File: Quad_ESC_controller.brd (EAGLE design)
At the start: 22.9 x 34 mm, 23 parts, among them Y1 ECS-80-S-4X

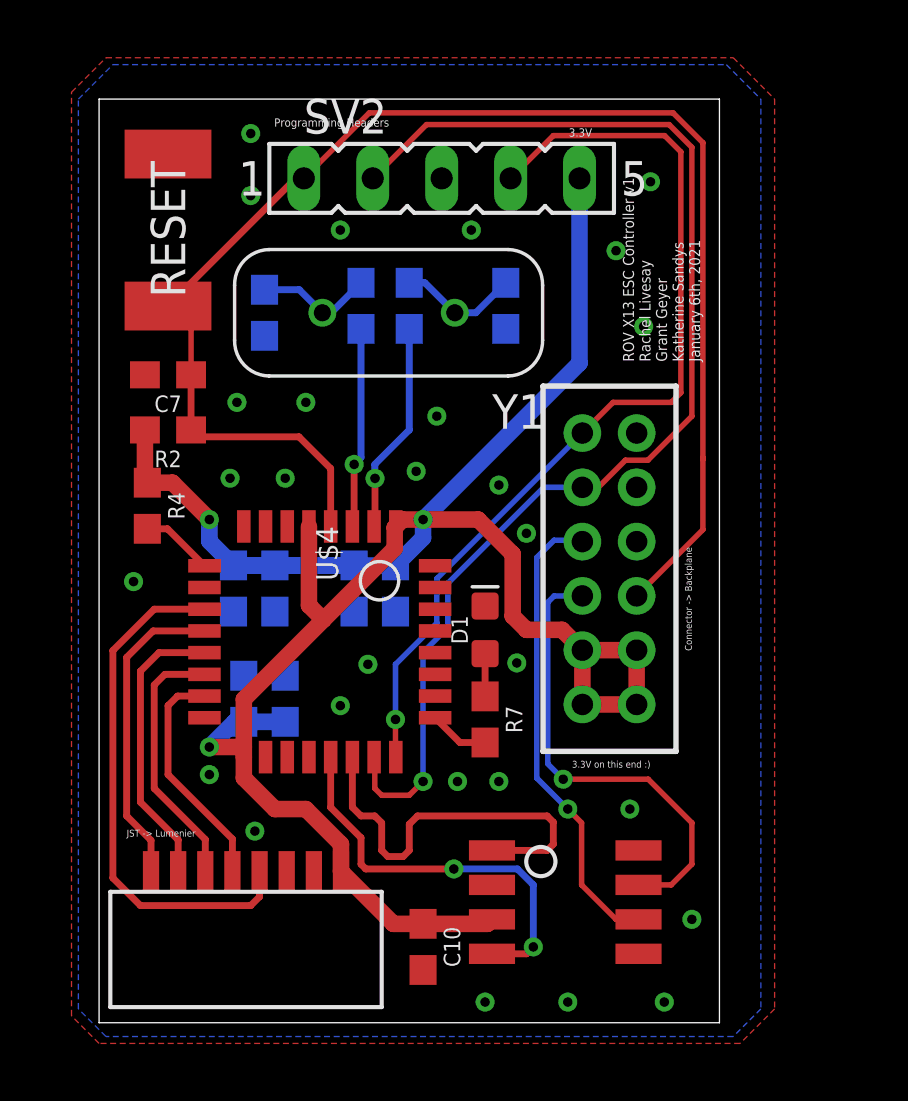
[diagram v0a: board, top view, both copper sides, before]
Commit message: Final Board Changes   ✽-(ˆ▿ˆ)/✽
thank god

(changes: vias con. to GND, esc id/tlm connections, design moved, connector footprint replaced, font sizes changed)
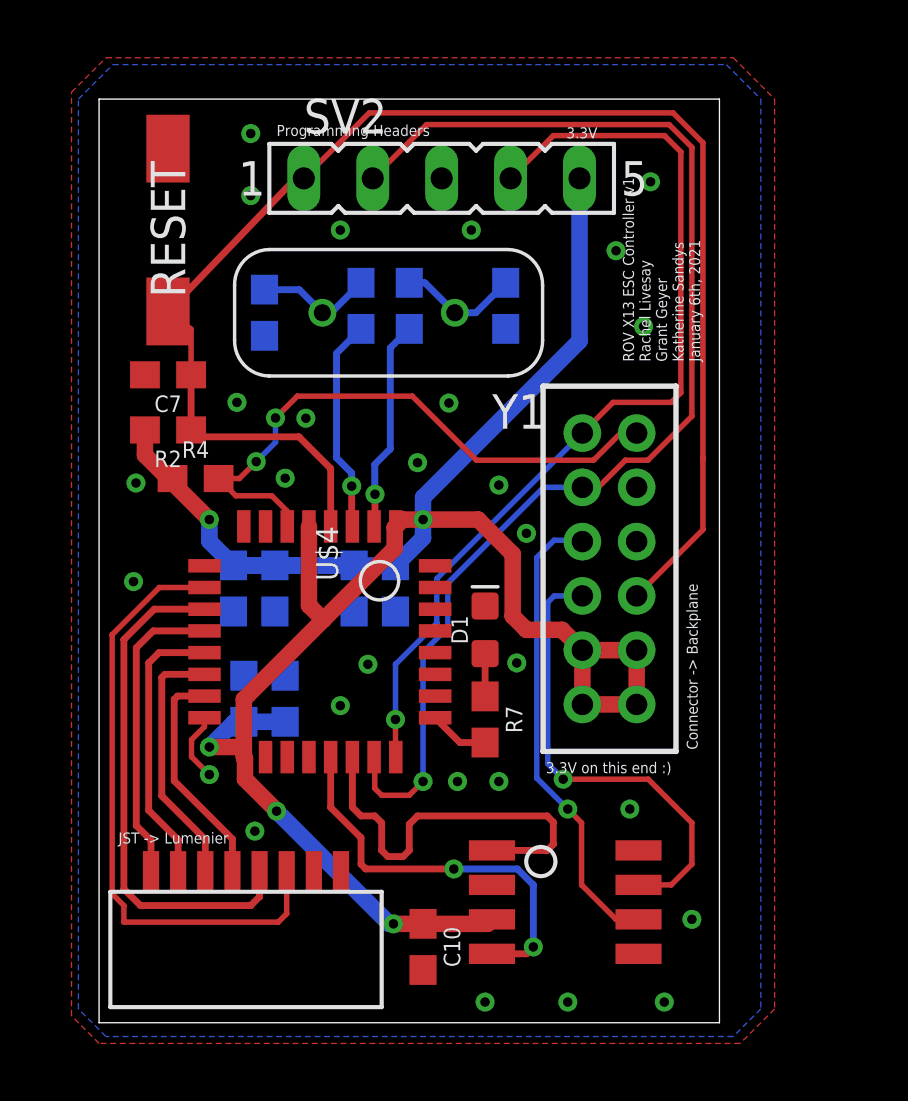
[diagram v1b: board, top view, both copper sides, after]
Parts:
- R7: value (none) -> 470
- RESET: value (none) -> DISCRETECOMPONENTS_SWITCH; device DiscreteComponents:SW_2512 -> Push button - FSM2JMTR:DISCRETECOMPONENTS_SW_2512
- U$3: value BACKPLANE_CONNECTORSBKP -> BACKPLANE_CONNECTORSESC; device BLHeli_32 45A:BACKPLANE_CONNECTORS_BKP -> BLHeli_32 45A:BACKPLANE_CONNECTORS_ESC
- moved R4 2.04 mm to (3.56, 20.1), turned to 0 degrees
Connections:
- removed net N$3: R4.2, U$4.PA3
- removed net N$7: U$3.8
- removed net N$8: U$3.12
- new net ADC: U$2.P$3, U$4.PA4
- new net ESC_ID: R4.2, U$3.12, U$4.PA0
- net +3V3: no longer U$2.P$1
- net GND: now also U$3.10; no longer U$2.P$3
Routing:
- net ADC: track 0.00 -> 22.6 mm
- net ESC_ID: track 0.00 -> 22.2 mm, vias 0 -> 2
- net N$3: track 2.67 -> 0.00 mm
- net GND: track 0.00 -> 2.56 mm, vias 0 -> 28
- net +3V3: track 85.9 -> 85.0 mm, vias 3 -> 5

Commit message: JST part
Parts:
- C10: value 100nF -> 0.1uF
- C8, C9: value 4.7uF -> 20pF
- R1, R3: value 1k -> 0
- U$2: value 8PIN_CONNECTOR -> JST-8PIN; device BLHeli_32 45A:8PI_CONNECTOR -> JST 8 pin:8PIN_CONNECTOR
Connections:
- net ADC: now also U$2.3; no longer U$2.P$3
- net GND: now also U$2.2; no longer U$2.P$2
- net TIM3_CH1: now also U$2.5; no longer U$2.P$5
- net TIM3_CH2: now also U$2.6; no longer U$2.P$6
- net TIM3_CH3: now also U$2.7; no longer U$2.P$7
- net TIM3_CH4: now also U$2.8; no longer U$2.P$8
- net TLM: now also U$2.4; no longer U$2.P$4

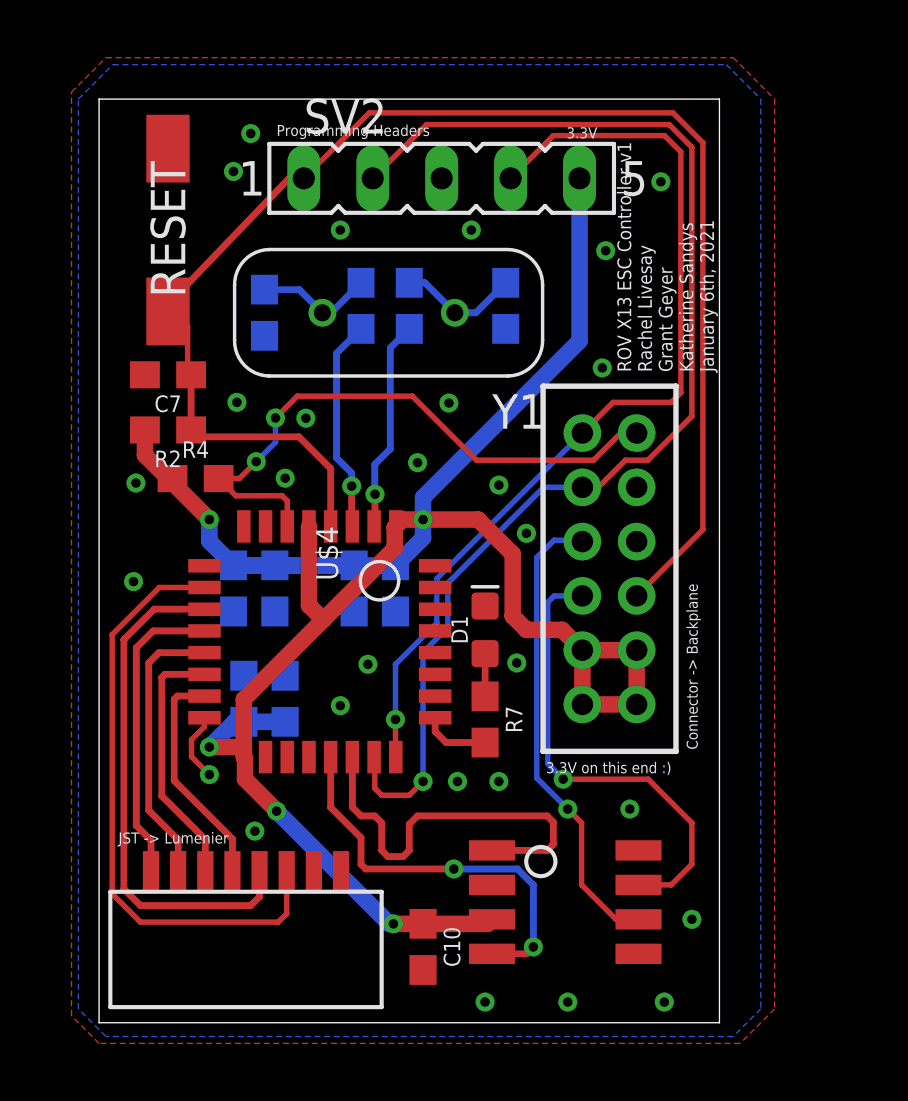
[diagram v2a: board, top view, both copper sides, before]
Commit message: Final Board Changes Pt. 2: Electric Boogaloo
Changes: [ bumped out board 100mil to the left, flipped esc signals on micro, moved TLM to analog pin 10 on micro, rotated connector, and rerouted board. ]
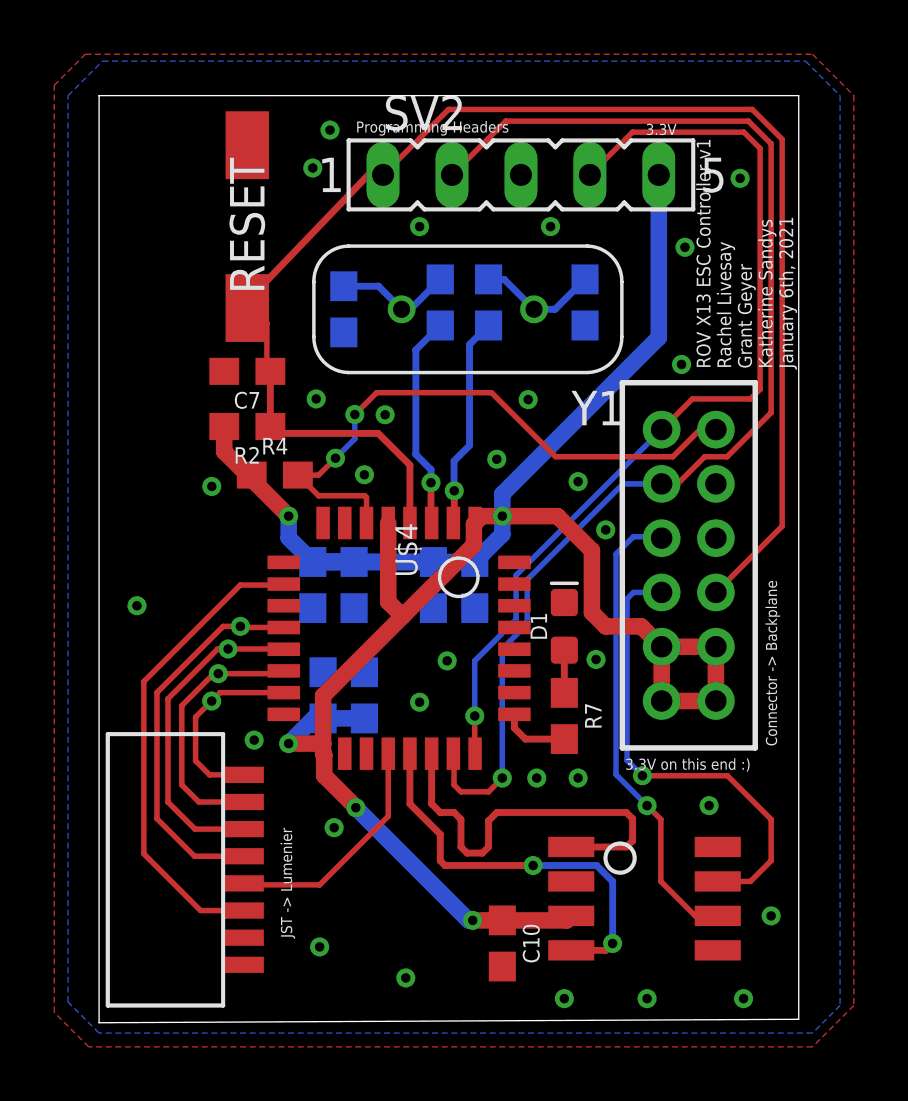
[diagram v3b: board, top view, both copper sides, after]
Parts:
- moved U$2 7.19 mm to (4.57, 0.64), turned to 90 degrees
- moved C3 2.92 mm to (12.3, 16.1)
- moved C4 2.92 mm to (8.26, 12.1)
- moved R1 2.92 mm to (12.6, 26.5)
- moved R3 2.92 mm to (14.4, 26.5)
- moved SV2 2.92 mm to (15.5, 31.2)
- moved U$4 2.92 mm to (8.26, 18.4)
- moved U$8 2.92 mm to (17.4, 2.67)
- moved Y1 2.92 mm to (13.6, 26.3)
- moved C2 2.92 mm to (9.78, 12.1)
- moved C7 2.92 mm to (5.46, 24.0)
- moved R2 2.92 mm to (5.46, 22.0)
- moved R4 2.92 mm to (6.48, 20.2)
- moved RESET 2.92 mm to (5.46, 29.3)
- moved C1 2.92 mm to (13.8, 16.1)
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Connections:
- net TIM3_CH1: now also U$4.PA6; no longer U$4.PB1
- net TIM3_CH2: now also U$4.PA7; no longer U$4.PB0
- net TIM3_CH3: now also U$4.PB0; no longer U$4.PA7
- net TIM3_CH4: now also U$4.PB1; no longer U$4.PA6
- net TLM: now also U$4.PA10; no longer U$4.PA5
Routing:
- net TLM: track 18.9 -> 8.71 mm
- net TIM3_CH1: track 8.39 -> 14.1 mm, vias 0 -> 1
- net ADC: track 22.2 -> 17.5 mm
- net TIM3_CH4: track 11.2 -> 7.21 mm, vias 0 -> 1
- net TIM3_CH2: track 9.43 -> 12.0 mm, vias 0 -> 1
- net GND: track 2.56 -> 0.00 mm, vias 28 -> 30
- net TIM3_CH3: track 10.3 -> 9.74 mm, vias 0 -> 1
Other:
- board size 22.9 x 34 mm -> 25.8 x 34.2 mm

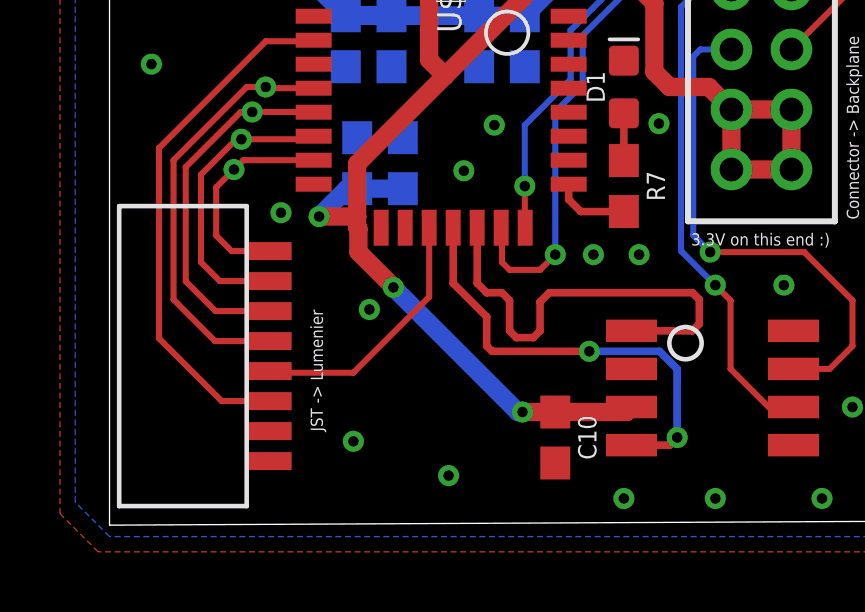
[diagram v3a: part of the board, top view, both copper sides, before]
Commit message: Added 1k Resistor TLM -> 3.3V
also tried airwiring it lol. it's v bad, but that is next year's problem.
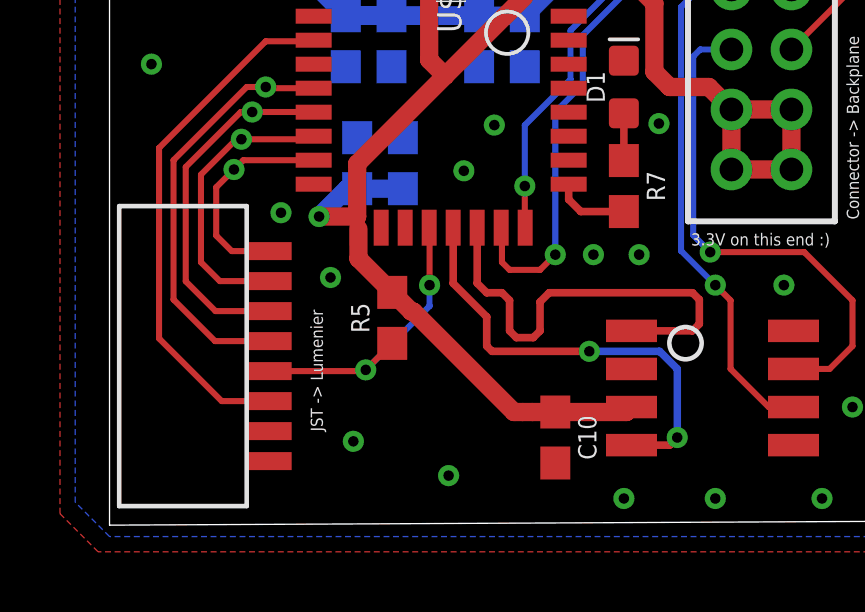
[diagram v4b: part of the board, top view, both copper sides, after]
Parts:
- added R5: 1k, SparkFun-Resistors:0603
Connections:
- net +3V3: now also R5.2
- net TLM: now also R5.1
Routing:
- net TLM: track 8.71 -> 10.2 mm, vias 0 -> 2
- net +3V3: track 85.0 -> 84.7 mm, vias 5 -> 3
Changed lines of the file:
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@@
 <element name="U$2" library="JST 8 pin" package="8PIN_CONNECTOR" package3d_urn="urn:adsk.eagle:package:25902943/3" value="JST-8PIN" x="4.572" y="0.635" smashed="yes" rot="R90"/>
 <element name="U$3" library="BLHeli_32 45A" package="BACKPLANE_CONNECTORS_ESC" value="BACKPLANE_CONNECTORSESC" x="21.73" y="16.856" smashed="yes"/>
+<element name="R5" library="SparkFun-Resistors" library_urn="urn:adsk.eagle:library:532" package="0603" package3d_urn="urn:adsk.eagle:package:39650/1" value="1k" x="9.4234" y="6.9088" smashed="yes" rot="R90">
+<attribute name="NAME" x="8.6614" y="6.9088" size="0.6096" layer="25" font="vector" ratio="20" rot="R90" align="bottom-center"/>
+<attribute name="PROD_ID" value=" " x="9.4234" y="6.9088" size="1.778" layer="27" rot="R90" display="off"/>
+<attribute name="VALUE" x="10.1854" y="6.9088" size="0.6096" layer="27" font="vector" ratio="20" rot="R90" align="top-center"/>
+</element>
 </elements>
 <signals>
@@
 </polygon>
 <contactref element="U$3" pad="10"/>
-<via x="8.6614" y="7.1882" extent="1-16" drill="0.35"/>
 <via x="1.397" y="15.367" extent="1-16" drill="0.35"/>
 <via x="4.1529" y="19.7612" extent="1-16" drill="0.35"/>
@@
 <signal name="+3V3">
 <contactref element="R2" pad="2"/>
-<contactref element="U$4" pad="VDDIO2"/>
 <contactref element="C2" pad="1"/>
 <contactref element="C4" pad="1"/>
@@
 <wire x1="13.813" y1="17.60458125" x2="13.813" y2="18.373" width="0.6096" layer="1"/>
 <wire x1="13.813" y1="18.373" x2="13.855" y2="18.415" width="0.6096" layer="1"/>
-<wire x1="8.255" y1="9.915" x2="8.255" y2="10.287" width="0.6096" layer="1"/>
 <wire x1="8.255" y1="10.287" x2="8.255" y2="12.04658125" width="0.6096" layer="1"/>
 <wire x1="8.255" y1="12.04658125" x2="11.185209375" y2="14.976790625" width="0.6096" layer="1"/>
@@
 <wire x1="6.985" y1="17.868" x2="6.985" y2="18.669" width="0.6096" layer="16"/>
 <via x="6.985" y="18.669" extent="1-16" drill="0.35"/>
-<wire x1="13.767" y1="3.771" x2="14.859" y2="3.771" width="0.6096" layer="1"/>
+<wire x1="13.767" y1="3.771" x2="14.097" y2="3.771" width="0.6096" layer="1"/>
+<wire x1="14.097" y1="3.771" x2="14.859" y2="3.771" width="0.6096" layer="1"/>
 <wire x1="17.399" y1="3.937" x2="17.233" y2="3.771" width="0.6096" layer="1"/>
 <wire x1="17.233" y1="3.771" x2="14.859" y2="3.771" width="0.6096" layer="1"/>
@@
 <wire x1="14.859" y1="18.669" x2="14.859" y2="19.4818" width="0.6096" layer="16"/>
 <wire x1="20.6248" y1="25.2476" x2="20.6248" y2="31.242" width="0.6096" layer="16"/>
-<via x="9.4615" y="7.9248" extent="1-16" drill="0.35"/>
-<wire x1="8.255" y1="9.915" x2="8.297" y2="9.873" width="0.6096" layer="1"/>
-<wire x1="8.297" y1="9.873" x2="8.297" y2="9.10458125" width="0.6096" layer="1"/>
-<wire x1="9.4615" y1="7.94008125" x2="9.4615" y2="7.9248" width="0.6096" layer="1"/>
-<wire x1="8.297" y1="9.10458125" x2="9.4615" y2="7.94008125" width="0.6096" layer="1"/>
-<wire x1="13.6153" y1="3.771" x2="13.767" y2="3.771" width="0.6096" layer="16"/>
-<via x="13.767" y="3.771" extent="1-16" drill="0.35"/>
-<wire x1="9.4615" y1="7.9248" x2="13.6153" y2="3.771" width="0.6096" layer="16"/>
 <contactref element="R4" pad="1"/>
 <wire x1="6.985" y1="18.669" x2="5.627" y2="20.027" width="0.6096" layer="1"/>
@@
 <wire x1="4.611" y1="21.971" x2="4.611" y2="21.043" width="0.6096" layer="1"/>
 <wire x1="4.611" y1="21.043" x2="5.627" y2="20.027" width="0.6096" layer="1"/>
+<contactref element="U$4" pad="VDDIO2"/>
+<contactref element="R5" pad="2"/>
+<wire x1="8.297" y1="8.8852" x2="9.4234" y2="7.7588" width="0.6096" layer="1"/>
+<wire x1="8.297" y1="9.873" x2="8.297" y2="8.8852" width="0.6096" layer="1"/>
+<wire x1="9.4234" y1="7.7588" x2="10.0654" y2="7.1168" width="0.6096" layer="1"/>
+<wire x1="10.0654" y1="7.1168" x2="10.13381875" y2="7.1168" width="0.6096" layer="1"/>
+<wire x1="13.47961875" y1="3.771" x2="13.767" y2="3.771" width="0.6096" layer="1"/>
+<wire x1="10.13381875" y1="7.1168" x2="13.47961875" y2="3.771" width="0.6096" layer="1"/>
+<wire x1="8.255" y1="9.915" x2="8.255" y2="11.215" width="0" layer="19" extent="1-16"/>
+<wire x1="8.297" y1="9.873" x2="8.255" y2="9.915" width="0" layer="19" extent="1-1"/>
 </signal>
 <signal name="CAN_TX">
@@
 <contactref element="U$4" pad="PA10"/>
 <wire x1="5.377" y1="5.08" x2="5.322" y2="5.135" width="0.2032" layer="1"/>
-<wire x1="10.655" y1="9.915" x2="10.655" y2="7.607" width="0.2032" layer="1"/>
-<wire x1="8.128" y1="5.08" x2="5.377" y2="5.08" width="0.2032" layer="1"/>
-<wire x1="10.655" y1="7.607" x2="8.128" y2="5.08" width="0.2032" layer="1"/>
+<contactref element="R5" pad="1"/>
+<wire x1="5.322" y1="5.135" x2="8.4996" y2="5.135" width="0.2032" layer="1"/>
+<wire x1="8.4996" y1="5.135" x2="8.5403" y2="5.1757" width="0.2032" layer="1"/>
+<wire x1="8.5403" y1="5.1757" x2="9.4234" y2="6.0588" width="0.2032" layer="1"/>
+<wire x1="10.655" y1="9.915" x2="10.668" y2="9.902" width="0.2032" layer="1"/>
+<wire x1="10.668" y1="9.902" x2="10.668" y2="8.001" width="0.2032" layer="1"/>
+<via x="10.668" y="8.001" extent="1-16" drill="0.35"/>
+<wire x1="10.668" y1="8.001" x2="10.668" y2="7.3034" width="0.2032" layer="16"/>
+<wire x1="10.668" y1="7.3034" x2="8.5403" y2="5.1757" width="0.2032" layer="16"/>
+<via x="8.5403" y="5.1757" extent="1-16" drill="0.35"/>
 </signal>
 <signal name="ADC">
@@
 <wire x1="3.739" y1="4.135" x2="5.322" y2="4.135" width="0.2032" layer="1"/>
 </signal>
+<signal name="N$3">
+<via x="7.366" y="8.255" extent="1-16" drill="0.35"/>
+</signal>
 </signals>
